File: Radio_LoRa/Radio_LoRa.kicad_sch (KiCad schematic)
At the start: 2 parts, among them J1 SMA-J-P-H-ST-EM1, U1 RFM95W-915S2

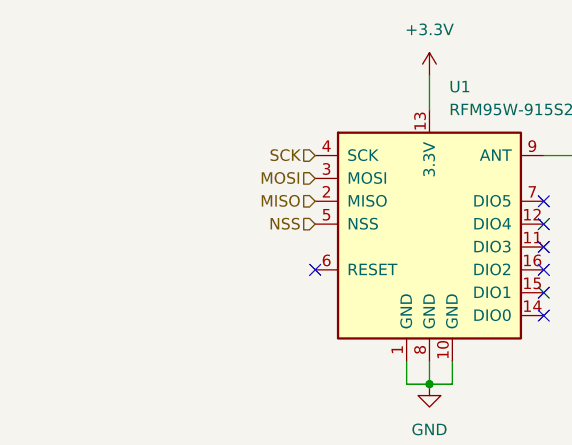
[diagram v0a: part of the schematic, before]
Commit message: Route sensors, IMU and radio board
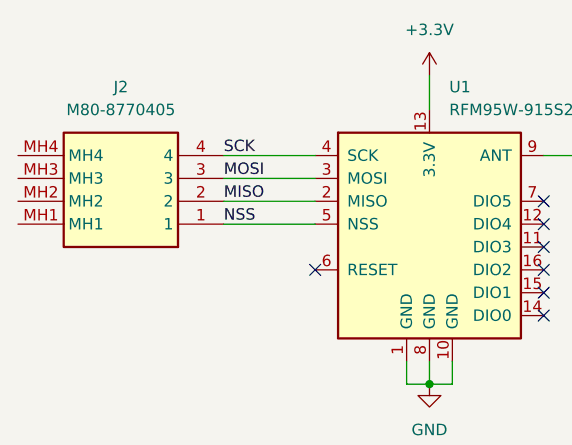
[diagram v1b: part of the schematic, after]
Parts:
- added J2: M80-8770405, M808770405, symbol M80-8770405:M80-8770405
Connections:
- net MISO: now also J2.2
- net MOSI: now also J2.3
- net NSS: now also J2.1
- net SCK: now also J2.4
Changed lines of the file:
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@@
+    (stroke (width 0) (type default))
+  )
+  (wire (pts (xy 128.27 95.25) (xy 138.43 95.25))
     (stroke (width 0) (type default))
   )
@@
     (stroke (width 0) (type default))
   )
+  (wire (pts (xy 128.27 97.79) (xy 138.43 97.79))
+    (stroke (width 0) (type default))
+  )
   (wire (pts (xy 153.67 120.65) (xy 151.13 120.65))
     (stroke (width 0) (type default))
@@
     (stroke (width 0) (type default))
   )
+  (wire (pts (xy 128.27 102.87) (xy 138.43 102.87))
+    (stroke (width 0) (type default))
+  )
+  (wire (pts (xy 128.27 100.33) (xy 138.43 100.33))
+    (stroke (width 0) (type default))
+  )
   (wire (pts (xy 173.99 97.79) (xy 173.99 102.87))
     (stroke (width 0) (type default))
   )
-  (hierarchical_label "MOSI" (shape input) (at 138.43 97.79 180) (fields_autoplaced)
-    (effects (font (size 1.27 1.27)) (justify right))
-  )
-  (hierarchical_label "MISO" (shape input) (at 138.43 100.33 180) (fields_autoplaced)
-    (effects (font (size 1.27 1.27)) (justify right))
-  )
-  (hierarchical_label "NSS" (shape input) (at 138.43 102.87 180) (fields_autoplaced)
-    (effects (font (size 1.27 1.27)) (justify right))
-  )
-  (hierarchical_label "SCK" (shape input) (at 138.43 95.25 180) (fields_autoplaced)
-    (effects (font (size 1.27 1.27)) (justify right))
+  (label "MOSI" (at 128.27 97.79 0) (fields_autoplaced)
+    (effects (font (size 1.27 1.27)) (justify left bottom))
+  )
+  (label "MISO" (at 128.27 100.33 0) (fields_autoplaced)
+    (effects (font (size 1.27 1.27)) (justify left bottom))
+  )
+  (label "SCK" (at 128.27 95.25 0) (fields_autoplaced)
+    (effects (font (size 1.27 1.27)) (justify left bottom))
+  )
+  (label "NSS" (at 128.27 102.87 0) (fields_autoplaced)
+    (effects (font (size 1.27 1.27)) (justify left bottom))
   )
   (symbol (lib_id "SMA-J-P-H-ST-EM1:SMA-J-P-H-ST-EM1") (at 176.53 97.79 0) (mirror y) (unit 1)
@@
         )
       )
+    )
+  )
+  (symbol (lib_id "M80-8770405:M80-8770405") (at 128.27 102.87 180) (unit 1)
+    (in_bom yes) (on_board yes) (dnp no) (fields_autoplaced)
+    (property "Reference" "J2" (at 116.84 87.63 0)
+      (effects (font (size 1.27 1.27)))
+    )
+    (property "Value" "M80-8770405" (at 116.84 90.17 0)
+      (effects (font (size 1.27 1.27)))
+    )
+    (property "Footprint" "M808770405" (at 109.22 7.95 0)
+      (effects (font (size 1.27 1.27)) (justify left top) hide)
+    )
+    (property "Datasheet" "https://cdn.harwin.com/pdfs/M80-877.pdf" (at 109.22 -92.05 0)
+      (effects (font (size 1.27 1.27)) (justify left top) hide)
+    )
+    (property "Height" "5.56" (at 109.22 -292.05 0)
+      (effects (font (size 1.27 1.27)) (justify left top) hide)
+    )
+    (property "Manufacturer_Name" "Harwin" (at 109.22 -392.05 0)
+      (effects (font (size 1.27 1.27)) (justify left top) hide)
+    )
+    (property "Manufacturer_Part_Number" "M80-8770405" (at 109.22 -492.05 0)
+      (effects (font (size 1.27 1.27)) (justify left top) hide)
+    )
+    (property "Mouser Part Number" "855-M80-8770405" (at 109.22 -592.05 0)
+      (effects (font (size 1.27 1.27)) (justify left top) hide)
+    )
+    (property "Mouser Price/Stock" "https://www.mouser.co.uk/ProductDetail/Harwin/M80-8770405?qs=3tymCvhQ29ZPq83M%252Bf8kIA%3D%3D" (at 109.22 -692.05 0)
+      (effects (font (size 1.27 1.27)) (justify left top) hide)
+    )
+    (property "Arrow Part Number" "" (at 109.22 -792.05 0)
+      (effects (font (size 1.27 1.27)) (justify left top) hide)
+    )
+    (property "Arrow Price/Stock" "" (at 109.22 -892.05 0)
+      (effects (font (size 1.27 1.27)) (justify left top) hide)
+    )
+    (pin "1")
+    (pin "2")
+    (pin "3")
+    (pin "4")
+    (pin "MH1")
+    (pin "MH2")
+    (pin "MH3")
+    (pin "MH4")
+    (instances
+      (project "Radio_LoRa"
+        (path "/1f7320e6-bd36-4aa9-bb78-0dd7fb23ef13"
+          (reference "J2") (unit 1)
+        )
+      )

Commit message: Done with most of the boards
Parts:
- added J3: M80-8770405, M808770405, symbol M80-8770405:M80-8770405
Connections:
- net +3.3V: now also J3.3
- net GND: now also J3.4
- net MISO: now also J2.1; no longer J2.2
- net MOSI: now also J2.2; no longer J2.3
- net NSS: now also J2.4; no longer J2.1
- net SCK: now also J2.3; no longer J2.4
- no-connect marks 7 -> 17
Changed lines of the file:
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@@
   (junction (at 151.13 120.65) (diameter 0) (color 0 0 0 0)
   )
+  (junction (at 151.13 87.63) (diameter 0) (color 0 0 0 0)
+  )
+  (no_connect (at 182.88 73.66))
   (no_connect (at 163.83 110.49))
   (no_connect (at 163.83 113.03))
   (no_connect (at 163.83 105.41))
+  (no_connect (at 105.41 97.79))
   (no_connect (at 163.83 100.33))
   (no_connect (at 138.43 107.95))
+  (no_connect (at 182.88 81.28))
+  (no_connect (at 182.88 78.74))
+  (no_connect (at 182.88 76.2))
+  (no_connect (at 105.41 100.33))
+  (no_connect (at 160.02 76.2))
+  (no_connect (at 105.41 95.25))
   (no_connect (at 163.83 107.95))
+  (no_connect (at 105.41 102.87))
   (no_connect (at 163.83 102.87))
+  (no_connect (at 160.02 73.66))
   (wire (pts (xy 148.59 120.65) (xy 151.13 120.65))
     (stroke (width 0) (type default))
   )
+  (wire (pts (xy 138.43 102.87) (xy 138.43 105.41))
+    (stroke (width 0) (type default))
+  )
+  (wire (pts (xy 152.4 78.74) (xy 152.4 87.63))
+    (stroke (width 0) (type default))
+  )
+  (wire (pts (xy 133.35 95.25) (xy 133.35 97.79))
+    (stroke (width 0) (type default))
+  )
+  (wire (pts (xy 138.43 95.25) (xy 133.35 95.25))
+    (stroke (width 0) (type default))
+  )
   (wire (pts (xy 151.13 118.11) (xy 151.13 120.65))
     (stroke (width 0) (type default))
   )
-  (wire (pts (xy 128.27 95.25) (xy 138.43 95.25))
+  (wire (pts (xy 151.13 87.63) (xy 151.13 90.17))
+    (stroke (width 0) (type default))
+  )
+  (wire (pts (xy 135.89 100.33) (xy 128.27 100.33))
+    (stroke (width 0) (type default))
+  )
+  (wire (pts (xy 128.27 102.87) (xy 137.16 102.87))
+    (stroke (width 0) (type default))
+  )
+  (wire (pts (xy 138.43 100.33) (xy 137.16 100.33))
+    (stroke (width 0) (type default))
+  )
+  (wire (pts (xy 138.43 97.79) (xy 135.89 97.79))
+    (stroke (width 0) (type default))
+  )
+  (wire (pts (xy 135.89 97.79) (xy 135.89 100.33))
     (stroke (width 0) (type default))
   )
@@
     (stroke (width 0) (type default))
   )
-  (wire (pts (xy 128.27 97.79) (xy 138.43 97.79))
+  (wire (pts (xy 133.35 97.79) (xy 128.27 97.79))
+    (stroke (width 0) (type default))
+  )
+  (wire (pts (xy 138.43 105.41) (xy 133.35 105.41))
     (stroke (width 0) (type default))
   )
@@
     (stroke (width 0) (type default))
   )
-  (wire (pts (xy 151.13 86.36) (xy 151.13 90.17))
-    (stroke (width 0) (type default))
-  )
-  (wire (pts (xy 128.27 102.87) (xy 138.43 102.87))
-    (stroke (width 0) (type default))
-  )
-  (wire (pts (xy 128.27 100.33) (xy 138.43 100.33))
+  (wire (pts (xy 151.13 86.36) (xy 151.13 87.63))
+    (stroke (width 0) (type default))
+  )
+  (wire (pts (xy 137.16 100.33) (xy 137.16 102.87))
     (stroke (width 0) (type default))
   )
@@
     (stroke (width 0) (type default))
   )
-  (label "MOSI" (at 128.27 97.79 0) (fields_autoplaced)
-    (effects (font (size 1.27 1.27)) (justify left bottom))
-  )
-  (label "MISO" (at 128.27 100.33 0) (fields_autoplaced)
-    (effects (font (size 1.27 1.27)) (justify left bottom))
-  )
-  (label "SCK" (at 128.27 95.25 0) (fields_autoplaced)
-    (effects (font (size 1.27 1.27)) (justify left bottom))
-  )
-  (label "NSS" (at 128.27 102.87 0) (fields_autoplaced)
+  (wire (pts (xy 160.02 81.28) (xy 160.02 82.55))
+    (stroke (width 0) (type default))
+  )
+  (wire (pts (xy 152.4 87.63) (xy 151.13 87.63))
+    (stroke (width 0) (type default))
+  )
+  (wire (pts (xy 160.02 78.74) (xy 152.4 78.74))
+    (stroke (width 0) (type default))
+  )
+  (label "MOSI" (at 128.27 100.33 0) (fields_autoplaced)
+    (effects (font (size 1.27 1.27)) (justify left bottom))
+  )
+  (label "MISO" (at 128.27 102.87 0) (fields_autoplaced)
+    (effects (font (size 1.27 1.27)) (justify left bottom))
+  )
+  (label "NSS" (at 133.35 105.41 0) (fields_autoplaced)
+    (effects (font (size 1.27 1.27)) (justify left bottom))
+  )
+  (label "SCK" (at 129.54 97.79 0) (fields_autoplaced)
+    (effects (font (size 1.27 1.27)) (justify left bottom))
+  )
+  (label "NSS" (at 128.27 95.25 0) (fields_autoplaced)
     (effects (font (size 1.27 1.27)) (justify left bottom))
   )
@@
     )
   )
+  (symbol (lib_id "M80-8770405:M80-8770405") (at 160.02 73.66 0) (unit 1)
+    (in_bom yes) (on_board yes) (dnp no)
+    (property "Reference" "J3" (at 171.45 88.9 0)
+      (effects (font (size 1.27 1.27)))
+    )
+    (property "Value" "M80-8770405" (at 171.45 86.36 0)
+      (effects (font (size 1.27 1.27)))
+    )
+    (property "Footprint" "M808770405" (at 179.07 168.58 0)
+      (effects (font (size 1.27 1.27)) (justify left top) hide)
+    )
+    (property "Datasheet" "https://cdn.harwin.com/pdfs/M80-877.pdf" (at 179.07 268.58 0)
+      (effects (font (size 1.27 1.27)) (justify left top) hide)
+    )
+    (property "Height" "5.56" (at 179.07 468.58 0)
+      (effects (font (size 1.27 1.27)) (justify left top) hide)
+    )
+    (property "Manufacturer_Name" "Harwin" (at 179.07 568.58 0)
+      (effects (font (size 1.27 1.27)) (justify left top) hide)
+    )
+    (property "Manufacturer_Part_Number" "M80-8770405" (at 179.07 668.58 0)
+      (effects (font (size 1.27 1.27)) (justify left top) hide)
+    )
+    (property "Mouser Part Number" "855-M80-8770405" (at 179.07 768.58 0)
+      (effects (font (size 1.27 1.27)) (justify left top) hide)
+    )
+    (property "Mouser Price/Stock" "https://www.mouser.co.uk/ProductDetail/Harwin/M80-8770405?qs=3tymCvhQ29ZPq83M%252Bf8kIA%3D%3D" (at 179.07 868.58 0)
+      (effects (font (size 1.27 1.27)) (justify left top) hide)
+    )
+    (property "Arrow Part Number" "" (at 179.07 968.58 0)
+      (effects (font (size 1.27 1.27)) (justify left top) hide)
+    )
+    (property "Arrow Price/Stock" "" (at 179.07 1068.58 0)
+      (effects (font (size 1.27 1.27)) (justify left top) hide)
+    )
+    (pin "1")
+    (pin "2")
+    (pin "3")
+    (pin "4")
+    (pin "MH1")
+    (pin "MH2")
+    (pin "MH3")
+    (pin "MH4")
+    (instances
+      (project "Radio_LoRa"
+        (path "/1f7320e6-bd36-4aa9-bb78-0dd7fb23ef13"
+          (reference "J3") (unit 1)
+        )
+      )
+    )
+  )
+  (symbol (lib_id "power:GND") (at 160.02 82.55 0) (unit 1)
+    (in_bom yes) (on_board yes) (dnp no) (fields_autoplaced)
+    (property "Reference" "#PWR04" (at 160.02 88.9 0)
+      (effects (font (size 1.27 1.27)) hide)
+    )
+    (property "Value" "GND" (at 160.02 87.63 0)
+      (effects (font (size 1.27 1.27)))
+    )
+    (property "Footprint" "" (at 160.02 82.55 0)
+      (effects (font (size 1.27 1.27)) hide)
+    )
+    (property "Datasheet" "" (at 160.02 82.55 0)
+      (effects (font (size 1.27 1.27)) hide)
+    )
+    (pin "1")
+    (instances
+      (project "Radio_LoRa"
+        (path "/1f7320e6-bd36-4aa9-bb78-0dd7fb23ef13"
+          (reference "#PWR04") (unit 1)
+        )
+      )
+      (project "Flight_Computer_V2"
+        (path "/39d7ebb3-b69d-4ae9-8f55-c9acfe77d345/172e0b61-5207-4042-aff3-940485c9496d"
+          (reference "#PWR010") (unit 1)
+        )
+      )
+      (project "Wireless com PCB"
+        (path "/9d6fe862-be9c-4405-9194-5c2bd78e94d8/0c9b6da0-8cf6-47f2-ad0c-512e5ab20d50"
+          (reference "#PWR046") (unit 1)
+        )
+      )
+    )
+  )
   (symbol (lib_id "power:+3.3V") (at 151.13 86.36 0) (unit 1)
     (in_bom yes) (on_board yes) (dnp no) (fields_autoplaced)
@@
   )
   (symbol (lib_id "M80-8770405:M80-8770405") (at 128.27 102.87 180) (unit 1)
-    (in_bom yes) (on_board yes) (dnp no) (fields_autoplaced)
+    (in_bom yes) (on_board yes) (dnp no)
     (property "Reference" "J2" (at 116.84 87.63 0)
       (effects (font (size 1.27 1.27)))

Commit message: LC24 PCBs
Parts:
- removed J2, J3: M80-8770405, M808770405, symbol M80-8770405:M80-8770405
- added H1, H2, H3, H4: MountingHole_Pad, Mounting_Wuerth:Mounting_Wuerth_WA-SMSI-M1.6_H1mm_9774010633, symbol Mechanical:MountingHole_Pad
- added J2: M80-8770422, Harwin-M80-8770422:CONN_M80-87704_HRW, symbol Harwin-M80-8770422:M80-8770422
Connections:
- net GND: now also H1.1, H2.1, H3.1, H4.1
- no-connect marks 17 -> 7
